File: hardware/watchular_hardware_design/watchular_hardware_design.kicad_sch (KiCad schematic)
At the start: 10 parts, among them U1 ESP32-C3FH4, U2 W25Q16JVSSIQ

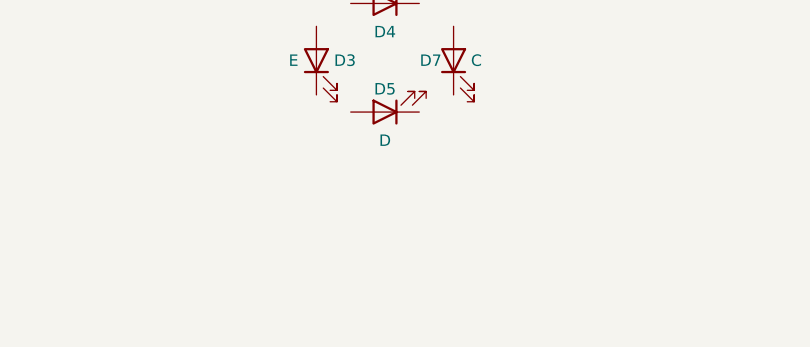
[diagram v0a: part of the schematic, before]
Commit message: Added LED driving resistor.
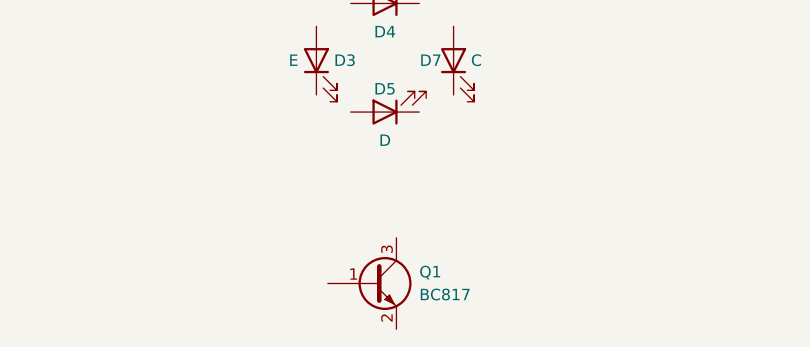
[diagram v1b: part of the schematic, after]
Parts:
- added Q1: BC817, Package_TO_SOT_SMD:SOT-23, symbol Transistor_BJT:BC817
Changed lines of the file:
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@@
     (pin "2")
+  )
+  (symbol (lib_id "Transistor_BJT:BC817") (at 153.67 137.16 0) (unit 1)
+    (in_bom yes) (on_board yes) (fields_autoplaced)
+    (property "Reference" "Q1" (id 0) (at 158.75 135.8899 0)
+      (effects (font (size 1.27 1.27)) (justify left))
+    )
+    (property "Value" "BC817" (id 1) (at 158.75 138.4299 0)
+      (effects (font (size 1.27 1.27)) (justify left))
+    )
+    (property "Footprint" "Package_TO_SOT_SMD:SOT-23" (id 2) (at 158.75 139.065 0)
+      (effects (font (size 1.27 1.27) italic) (justify left) hide)
+    )
+    (property "Datasheet" "https://www.onsemi.com/pub/Collateral/BC818-D.pdf" (id 3) (at 153.67 137.16 0)
+      (effects (font (size 1.27 1.27)) (justify left) hide)
+    )
+    (pin "1")
+    (pin "2")
+    (pin "3")
   )
   (symbol (lib_id "power:+3.3V") (at 106.68 35.56 0) (unit 1)
@@
       (reference "D7") (unit 1) (value "C") (footprint "LED_SMD:LED_0603_1608Metric")
     )
+    (path "/ae584ec4-b999-4071-8f7c-d778610a0704"
+      (reference "Q1") (unit 1) (value "BC817") (footprint "Package_TO_SOT_SMD:SOT-23")
+    )
     (path "/e238c8f6-f81c-451c-b083-2e5d79bf81d5"

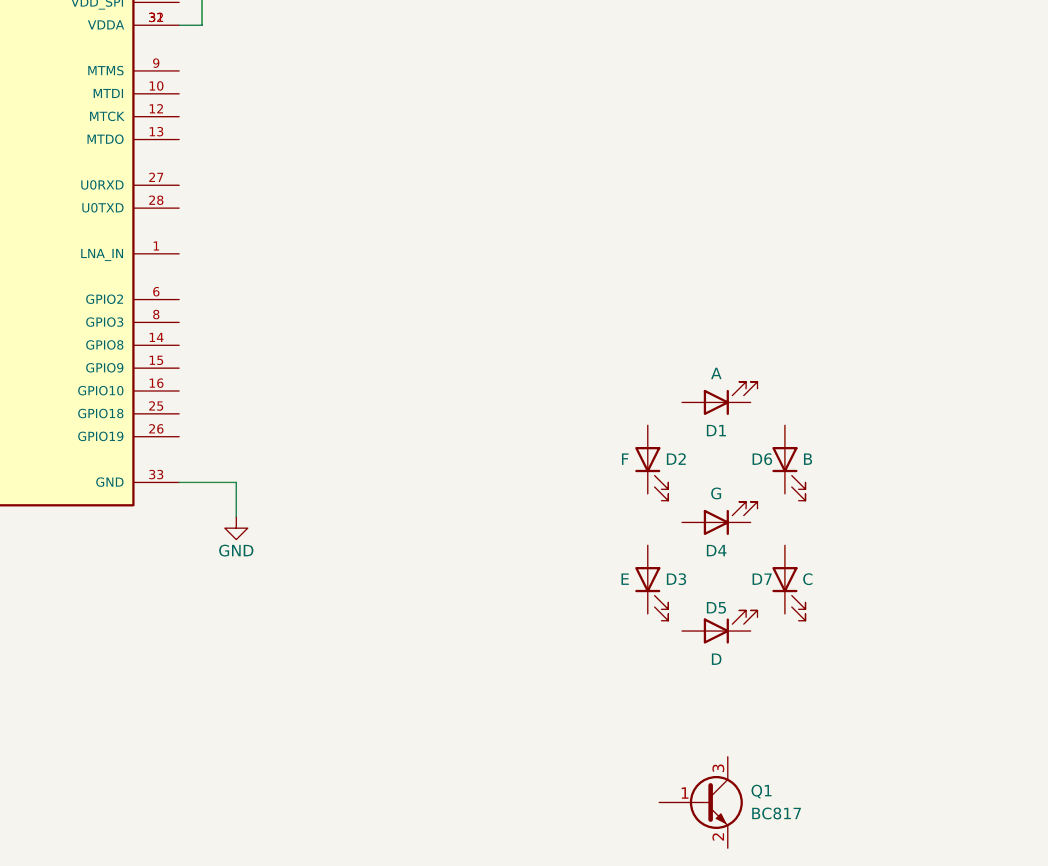
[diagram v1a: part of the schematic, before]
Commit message: Added resistors for the LEDs but alrady running into the IO count problem.
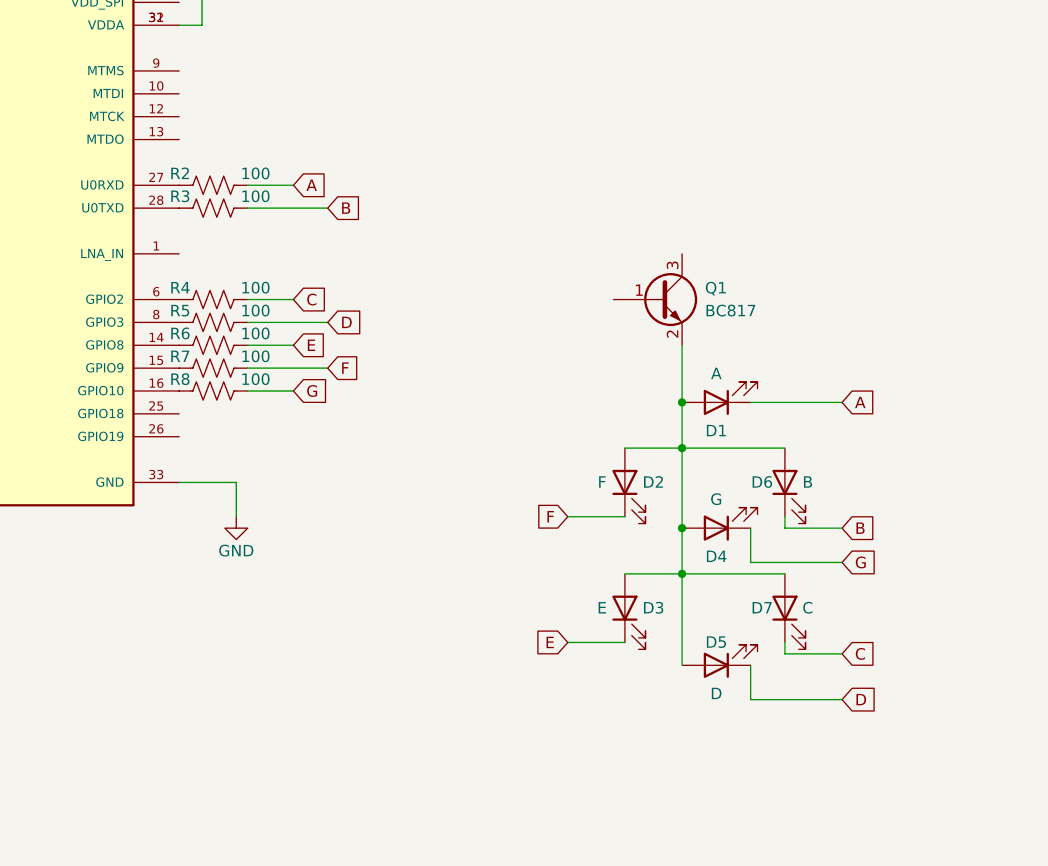
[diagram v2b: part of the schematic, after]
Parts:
- added R2, R3, R4, R5, R6, R7, R8: 100, Resistor_SMD:R_0402_1005Metric, symbol Device:R_US
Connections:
- net E: now reaches D3.1 (K)
- net E: now also R6.2
- net at D3.2 (A): now also D1.2 (A), D2.2 (A), D4.2 (A), D5.2 (A), D6.2 (A), D7.2 (A), Q1.2 (E)
- net A: now reaches D1.1 (K)
- net A: now also R2.2
- net D: now reaches D5.1 (K)
- net D: now also R5.2
- net C: now reaches D7.1 (K)
- net C: now also R4.2
- net G: now reaches D4.1 (K)
- net G: now also R8.2
- net F: now reaches D2.1 (K)
- net F: now also R7.2
- net B: now reaches D6.1 (K)
- net B: now also R3.2
- net at U1.14 (GPIO8): now also R6.1
- net at U1.15 (GPIO9): now also R7.1
- net at U1.16 (GPIO10): now also R8.1
- net at U1.27 (U0RXD): now also R2.1
- net at U1.28 (U0TXD): now also R3.1
- net at U1.6 (GPIO2): now also R4.1
- net at U1.8 (GPIO3): now also R5.1
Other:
- company: lilordag -> Lilordag
- title: Broys - 4 x 7 seven segment display -> Watchular - 4 x 7 seven segment display
- moved on the sheet: D2, D3, D4, D5, D6, D7, Q1

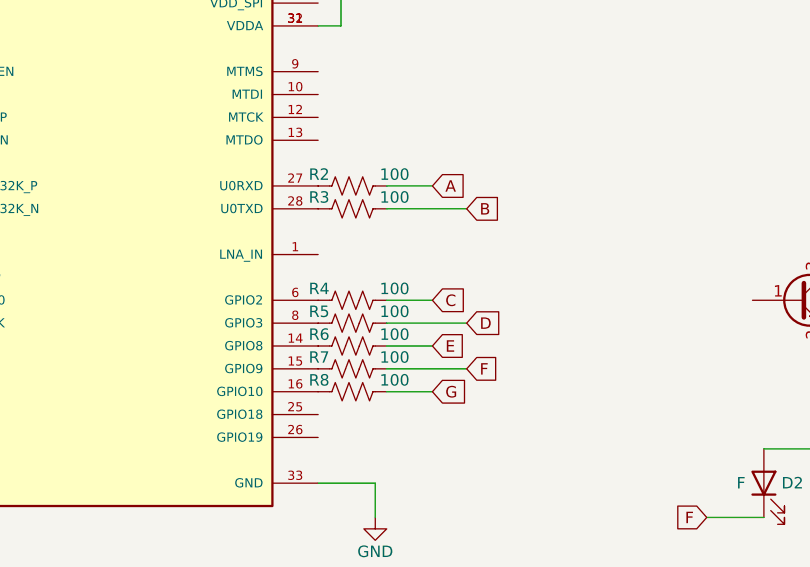
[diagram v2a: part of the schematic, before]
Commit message: Configured boot strapping pins
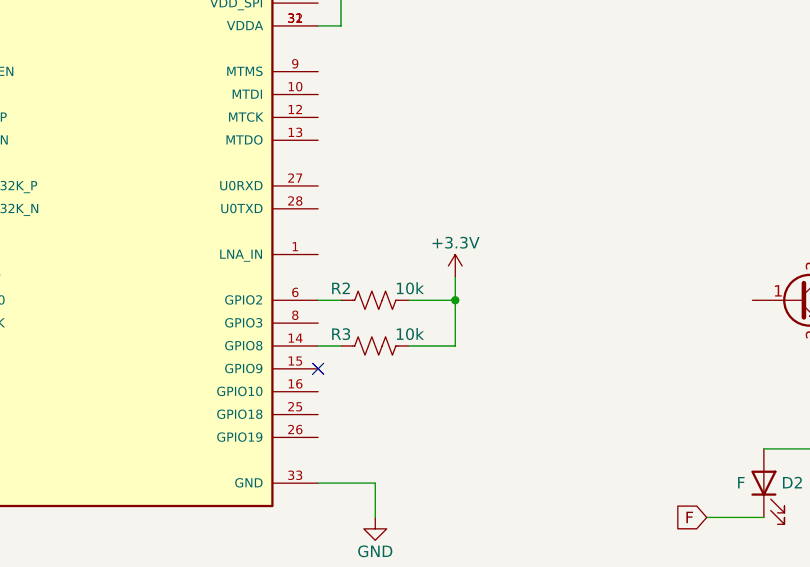
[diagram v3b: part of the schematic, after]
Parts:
- removed R4, R5, R6, R7, R8: 100, Resistor_SMD:R_0402_1005Metric, symbol Device:R_US
- R2, R3: value 100 -> 10k
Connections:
- net +3V3: now also R2.2, R3.2
- net A: no longer R2.2
- net B: no longer R3.2
- net at R3.1: now also U1.14 (GPIO8); no longer U1.28 (U0TXD)
- net at U1.6 (GPIO2): now also R2.1
- net at U1.27 (U0RXD): no longer R2.1
- no-connect marks 2 -> 3

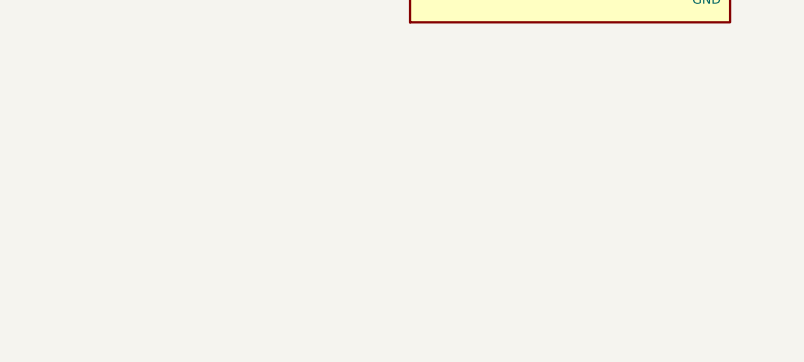
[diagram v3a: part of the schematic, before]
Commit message: Added ceramic chip antenna to the project.
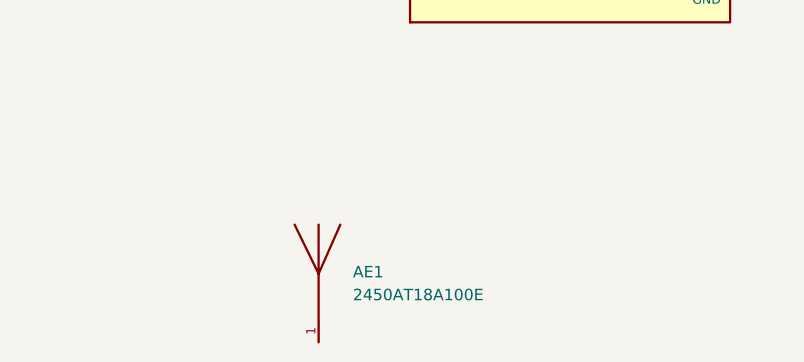
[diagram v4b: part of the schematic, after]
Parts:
- added AE1: 2450AT18A100E, ANTC3216X140N, symbol 2450AT18A100E:2450AT18A100E
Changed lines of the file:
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@@
+    (pin "1")
+  )
+  (symbol (lib_id "2450AT18A100E:2450AT18A100E") (at 44.45 134.62 0) (unit 1)
+    (in_bom yes) (on_board yes) (fields_autoplaced)
+    (property "Reference" "AE1" (id 0) (at 48.26 131.8894 0)
+      (effects (font (size 1.27 1.27)) (justify left))
+    )
+    (property "Value" "2450AT18A100E" (id 1) (at 48.26 134.4294 0)
+      (effects (font (size 1.27 1.27)) (justify left))
+    )
+    (property "Footprint" "ANTC3216X140N" (id 2) (at 44.45 134.62 0)
+      (effects (font (size 1.27 1.27)) (justify left bottom) hide)
+    )
+    (property "Datasheet" "" (id 3) (at 44.45 134.62 0)
+      (effects (font (size 1.27 1.27)) (justify left bottom) hide)
+    )
+    (property "STANDARD" "IPC-7351B" (id 4) (at 44.45 134.62 0)
+      (effects (font (size 1.27 1.27)) (justify left bottom) hide)
+    )
+    (property "PARTREV" "1.3" (id 5) (at 44.45 134.62 0)
+      (effects (font (size 1.27 1.27)) (justify left bottom) hide)
+    )
+    (property "MANUFACTURER" "JOHANSON DESIGN" (id 6) (at 44.45 134.62 0)
+      (effects (font (size 1.27 1.27)) (justify left bottom) hide)
+    )
     (pin "1")
   )
@@
       (reference "#PWR07") (unit 1) (value "+3.3V") (footprint "")
     )
+    (path "/1139fd41-bcfc-4cbe-8f9a-b980537f1914"
+      (reference "AE1") (unit 1) (value "2450AT18A100E") (footprint "ANTC3216X140N")
+    )
     (path "/2a85eac6-ce98-4719-81e9-43d8fbb9d534"

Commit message: Added antenna to the MCU
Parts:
- added C1: 1pF, Capacitor_SMD:C_0402_1005Metric, symbol Device:C
- added L1: 2.7 nH, Inductor_SMD:L_0402_1005Metric, symbol Device:L_Small
- added L2: 3.9 nH, Inductor_SMD:L_0402_1005Metric, symbol Device:L_Small
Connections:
- net GND: now also L1.1
- net at AE1.1: now also L2.2
- net antenna: now reaches U1.1 (LNA_IN)
- net antenna: now also C1.1
- new net: C1.2, L1.2, L2.1
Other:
- note added: "Antenna (BT + WIFI)"
- moved on the sheet: AE1

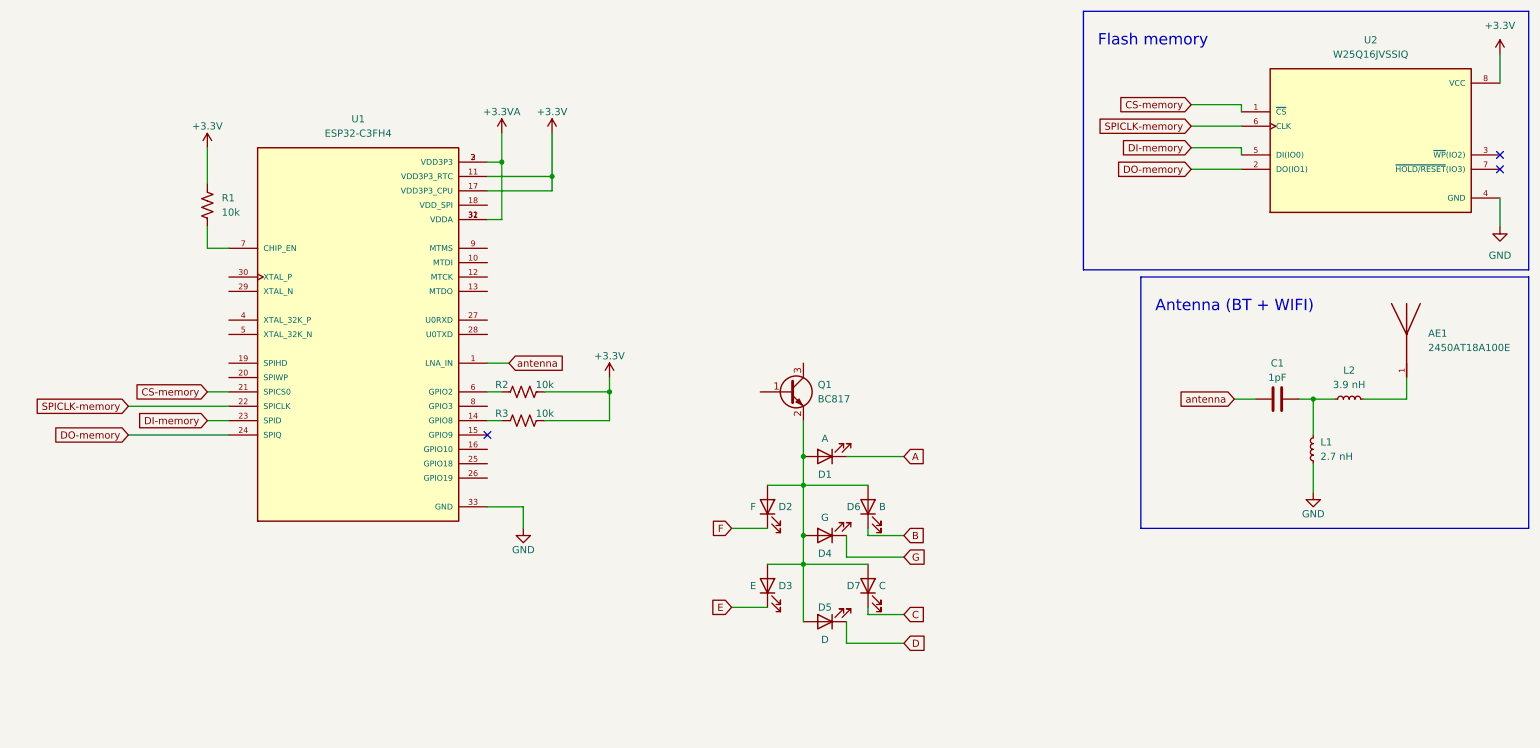
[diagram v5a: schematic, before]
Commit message: Made analog filter for VDD3P3.
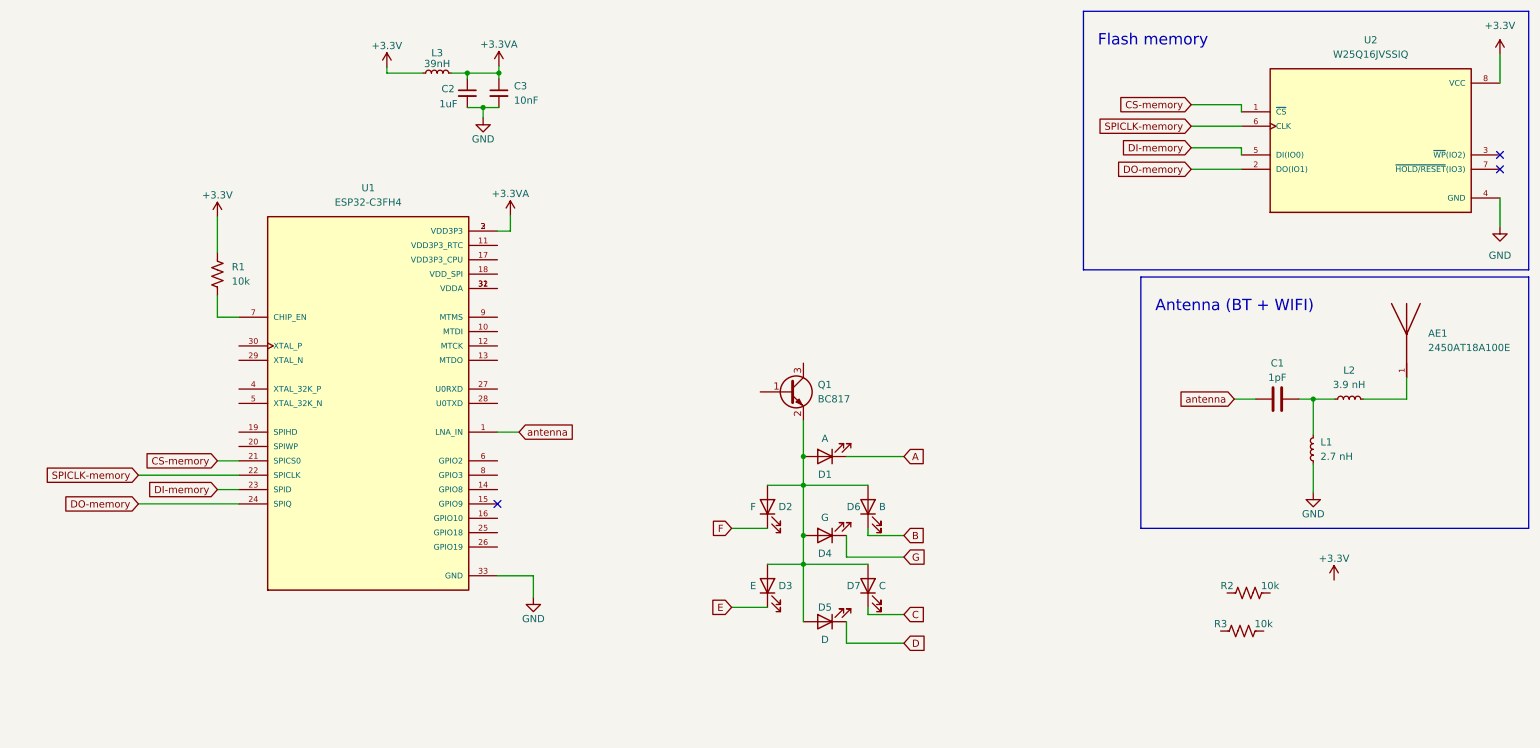
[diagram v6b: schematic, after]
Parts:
- added C2: 1uF, Inductor_SMD:L_0402_1005Metric, symbol Device:C_Small
- added C3: 10nF, Inductor_SMD:L_0402_1005Metric, symbol Device:C_Small
- added L3: 39nH, Inductor_SMD:L_0402_1005Metric, symbol Device:L_Small
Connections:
- net +3.3VA: now also C2.1, C3.1, L3.2; no longer U1.31 (VDDA), U1.32 (VDDA)
- net +3V3: now also L3.1; no longer R2.2, R3.2, U1.11 (VDD3P3_RTC), U1.17 (VDD3P3_CPU)
- net GND: now also C2.2, C3.2
- net at R2.1: no longer U1.6 (GPIO2)
- net at R3.1: no longer U1.14 (GPIO8)
- new net: U1.31 (VDDA), U1.32 (VDDA)
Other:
- moved on the sheet: R1, R2, R3, U1
